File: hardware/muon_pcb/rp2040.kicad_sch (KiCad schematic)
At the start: 36 parts, among them J4 Micro_SD_Card_Det1, J5 Conn_01x02_Pin, SW4 SW_Push_Shielded, SW5 SW_Push_Shielded, U12 RP2040, U3 W25Q128JVS, Y3 ABM8-272-T3

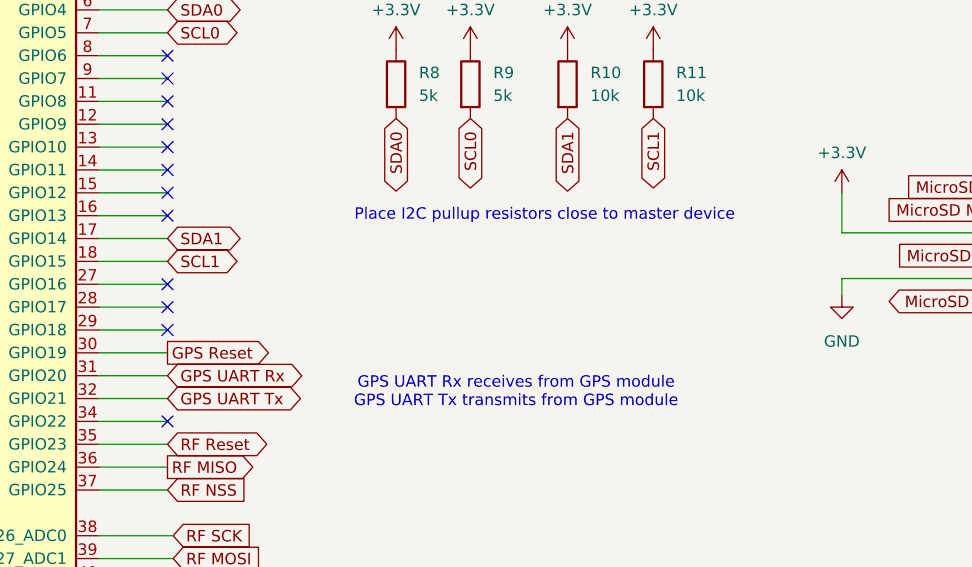
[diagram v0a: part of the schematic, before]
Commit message: uploaded preliminary pcb layout
need to research components to use (resistors & package size), buttons, test points, LEDs). also need to ask zach which ferrite bead he picked and about battery holder.
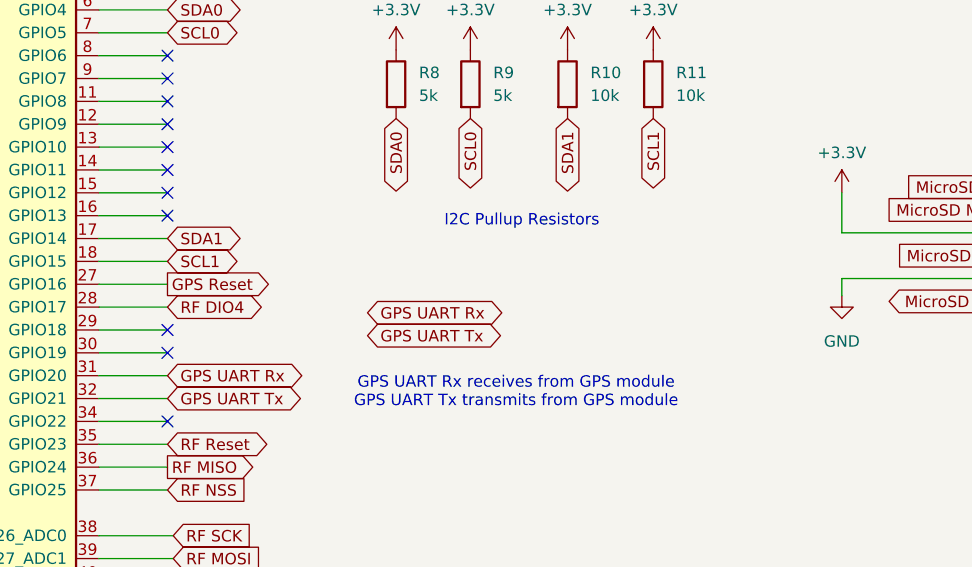
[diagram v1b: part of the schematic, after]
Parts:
- C1, C2: footprint Capacitor_SMD:C_0603_1608Metric -> Capacitor_SMD:C_0402_1005Metric
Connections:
- net GPS Reset: now also U12.27 (GPIO16); no longer U12.30 (GPIO19)
- net RF DIO4: now reaches U12.28 (GPIO17)
- no-connect marks 16 -> 15
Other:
- note added: "I2C Pullup Resistors"
- note removed: "Place I2C pullup resistors close to master device"
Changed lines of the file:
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@@
 	(generator_version "9.0")
 	(paper "A4")
-	(text "Place I2C pullup resistors close to master device"
-		(exclude_from_sim no)
-		(at 167.005 128.905 0)
-		(effects
-			(font
-				(size 1.27 1.27)
-			)
-		)
-	)
 	(text "Make sure C10 is close to pin 44 of RP2040"
 		(exclude_from_sim no)
@@
 		)
 	)
+	(text "I2C Pullup Resistors"
+		(exclude_from_sim no)
+		(at 164.465 129.54 0)
+		(effects
+			(font
+				(size 1.27 1.27)
+			)
+		)
+	)
 	(text "make sure diode used is\nexactly same one as used in proves kit"
 		(exclude_from_sim no)
@@
 	)
 	(no_connect
-		(at 125.095 136.525)
-	)
-	(no_connect
-		(at 125.095 139.065)
-	)
-	(no_connect
 		(at 125.095 123.825)
 	)
@@
 	)
 	(no_connect
+		(at 125.095 144.145)
+	)
+	(no_connect
 		(at 227.33 123.19)
 	)
@@
 		)
 	)
+	(global_label "RF DIO4"
+		(shape bidirectional)
+		(at 125.095 139.065 0)
+		(fields_autoplaced yes)
+		(effects
+			(font
+				(size 1.27 1.27)
+			)
+			(justify left)
+		)
+		(property "Intersheetrefs" "${INTERSHEET_REFS}"
+			(at 136.9325 139.065 0)
+			(effects
+				(font
+					(size 1.27 1.27)
+				)
+				(justify left)
+				(hide yes)
+			)
+		)
+	)
 	(global_label "RF SCK"
 		(shape input)
@@
 		)
 	)
-	(global_label "USB_DM"
-		(shape bidirectional)
-		(at 136.525 88.265 0)
+	(global_label "GPS Reset"
+		(shape output)
+		(at 125.095 136.525 0)
 		(fields_autoplaced yes)
 		(effects
 			(font
 				(size 1.27 1.27)
-				(thickness 0.1588)
 			)
 			(justify left)
 		)
 		(property "Intersheetrefs" "${INTERSHEET_REFS}"
-			(at 148.1205 88.265 0)
+			(at 137.9983 136.525 0)
 			(effects
 				(font
@@
 		)
 	)
-	(global_label "GPS Reset"
-		(shape output)
-		(at 125.095 144.145 0)
+	(global_label "USB_DM"
+		(shape bidirectional)
+		(at 136.525 88.265 0)
 		(fields_autoplaced yes)
 		(effects
 			(font
 				(size 1.27 1.27)
+				(thickness 0.1588)
 			)
 			(justify left)
 		)
 		(property "Intersheetrefs" "${INTERSHEET_REFS}"
-			(at 137.9983 144.145 0)
+			(at 148.1205 88.265 0)
 			(effects
 				(font
@@
 		)
 	)
+	(global_label "GPS UART Tx"
+		(shape bidirectional)
+		(at 147.32 142.24 0)
+		(fields_autoplaced yes)
+		(effects
+			(font
+				(size 1.27 1.27)
+			)
+			(justify left)
+		)
+		(property "Intersheetrefs" "${INTERSHEET_REFS}"
+			(at 163.7536 142.24 0)
+			(effects
+				(font
+					(size 1.27 1.27)
+				)
+				(justify left)
+				(hide yes)
+			)
+		)
+	)
 	(global_label "MicroSD CS"
 		(shape output)
@@
 		)
 	)
+	(global_label "GPS UART Rx"
+		(shape bidirectional)
+		(at 147.32 139.7 0)
+		(fields_autoplaced yes)
+		(effects
+			(font
+				(size 1.27 1.27)
+			)
+			(justify left)
+		)
+		(property "Intersheetrefs" "${INTERSHEET_REFS}"
+			(at 164.056 139.7 0)
+			(effects
+				(font
+					(size 1.27 1.27)
+				)
+				(justify left)
+				(hide yes)
+			)
+		)
+	)
 	(global_label "MicroSD CLK"
 		(shape input)
@@
 			)
 		)
-		(property "Footprint" "Capacitor_SMD:C_0603_1608Metric"
+		(property "Footprint" "Capacitor_SMD:C_0402_1005Metric"
 			(at 53.6702 74.295 0)
 			(effects
@@
 			)
 		)
-		(property "Footprint" "Capacitor_SMD:C_0603_1608Metric"
+		(property "Footprint" "Capacitor_SMD:C_0402_1005Metric"
 			(at 117.8052 73.025 0)
 			(effects

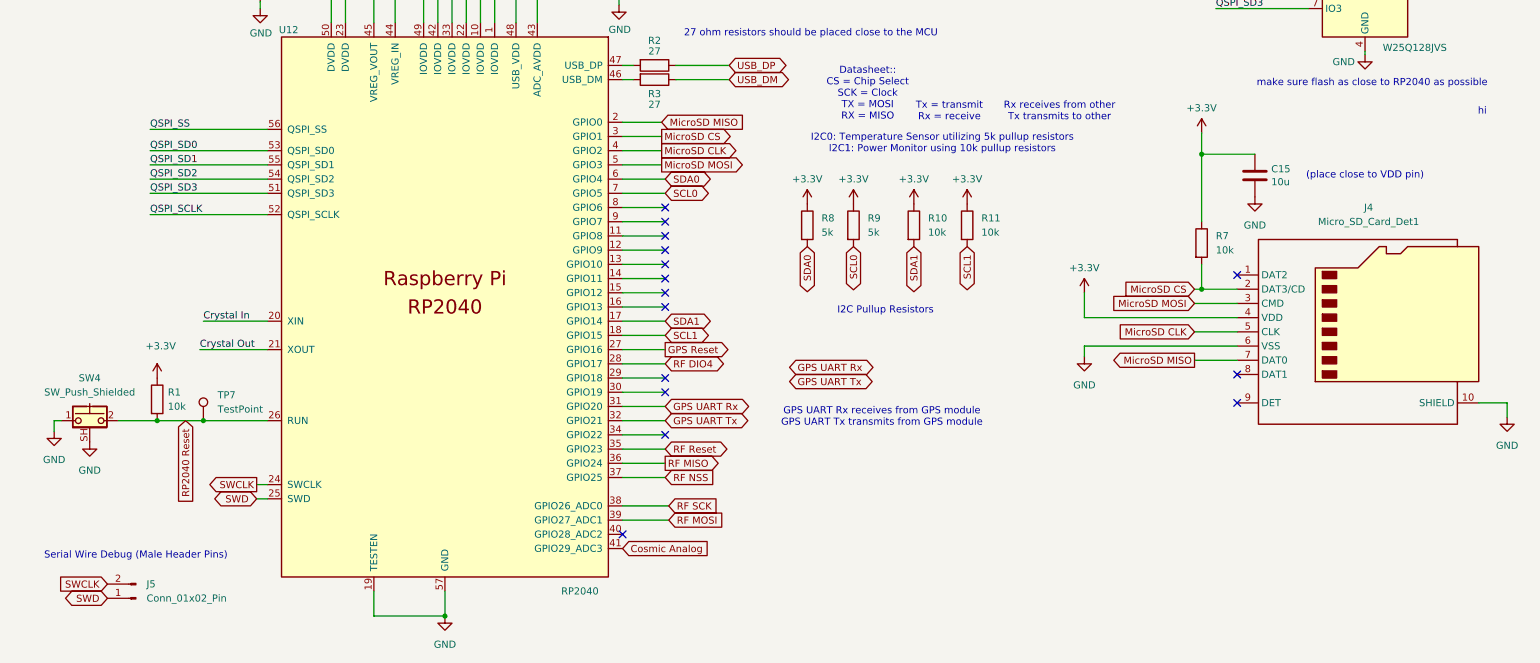
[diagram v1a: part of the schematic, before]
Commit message: uploaded pcb layout using proves edge cuts
-proves edge cuts with mounting holes
-added credits
-used correct sizes for resistors (based on components picked for resistors)
-to do: pick button, put in df11 connector to supply 5V, determine led being used and resistor values, make sure led wont explode
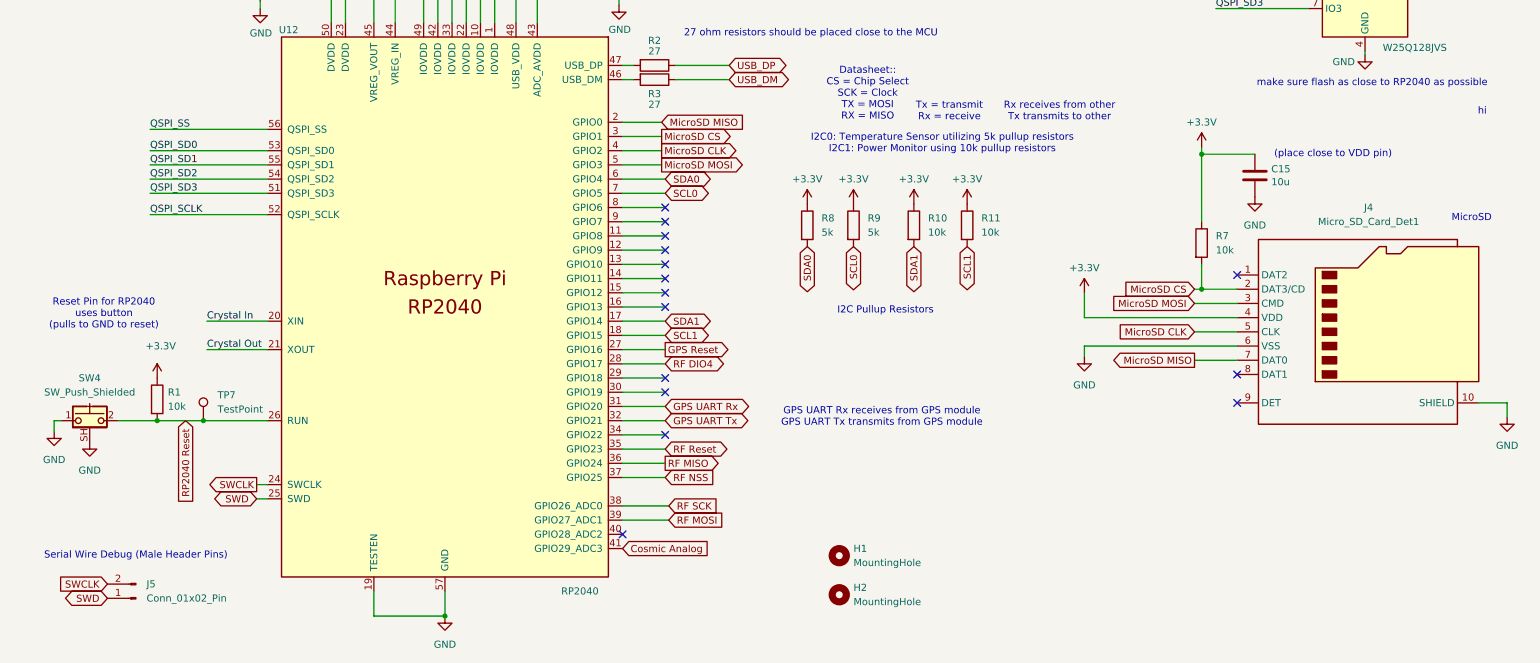
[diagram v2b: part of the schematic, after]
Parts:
- added H1, H2: MountingHole, symbol Mechanical:MountingHole
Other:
- note added: "MicroSD"
- note added: "Reset Pin for RP2040 uses button (pulls to GND to reset)"
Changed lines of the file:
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@@
 		)
 	)
+	(text "MicroSD"
+		(exclude_from_sim no)
+		(at 269.24 113.03 0)
+		(effects
+			(font
+				(size 1.27 1.27)
+			)
+		)
+	)
+	(text "Reset Pin for RP2040 \nuses button\n(pulls to GND to reset)"
+		(exclude_from_sim no)
+		(at 24.765 130.175 0)
+		(effects
+			(font
+				(size 1.27 1.27)
+			)
+		)
+	)
 	(text "make sure flash as close to RP2040 as possible"
 		(exclude_from_sim no)
@@
 	(text "(place close to VDD pin)"
 		(exclude_from_sim no)
-		(at 250.19 105.41 0)
+		(at 244.475 101.6 0)
 		(effects
 			(font
@@
 	(wire
 		(pts
-			(xy 220.98 97.79) (xy 220.98 101.6)
+			(xy 220.98 100.33) (xy 220.98 101.6)
 		)
 		(stroke
@@
 	(wire
 		(pts
-			(xy 42.545 131.445) (xy 53.975 131.445)
+			(xy 43.18 131.445) (xy 53.975 131.445)
 		)
 		(stroke
@@
 	(wire
 		(pts
-			(xy 41.91 136.525) (xy 53.975 136.525)
+			(xy 43.18 136.525) (xy 53.975 136.525)
 		)
 		(stroke
@@
 	)
 	(label "Crystal Out"
-		(at 41.91 136.525 0)
+		(at 43.18 136.525 0)
 		(effects
 			(font
@@
 	)
 	(label "Crystal In"
-		(at 42.545 131.445 0)
+		(at 43.18 131.445 0)
 		(effects
 			(font
@@
 		)
 	)
-	(global_label "GPS UART Tx"
-		(shape bidirectional)
-		(at 147.32 142.24 0)
-		(fields_autoplaced yes)
-		(effects
-			(font
-				(size 1.27 1.27)
-			)
-			(justify left)
-		)
-		(property "Intersheetrefs" "${INTERSHEET_REFS}"
-			(at 163.7536 142.24 0)
-			(effects
-				(font
-					(size 1.27 1.27)
-				)
-				(justify left)
-				(hide yes)
-			)
-		)
-	)
 	(global_label "MicroSD CS"
 		(shape output)
@@
 		)
 	)
-	(global_label "GPS UART Rx"
-		(shape bidirectional)
-		(at 147.32 139.7 0)
-		(fields_autoplaced yes)
-		(effects
-			(font
-				(size 1.27 1.27)
-			)
-			(justify left)
-		)
-		(property "Intersheetrefs" "${INTERSHEET_REFS}"
-			(at 164.056 139.7 0)
-			(effects
-				(font
-					(size 1.27 1.27)
-				)
-				(justify left)
-				(hide yes)
-			)
-		)
-	)
 	(global_label "MicroSD CLK"
 		(shape input)
@@
 	)
 	(symbol
+		(lib_id "Mechanical:MountingHole")
+		(at 156.21 180.34 0)
+		(unit 1)
+		(exclude_from_sim yes)
+		(in_bom no)
+		(on_board yes)
+		(dnp no)
+		(fields_autoplaced yes)
+		(property "Reference" "H2"
+			(at 158.75 179.0699 0)
+			(effects
+				(font
+					(size 1.27 1.27)
+				)
+				(justify left)
+			)
+		)
+		(property "Value" "MountingHole"
+			(at 158.75 181.6099 0)
+			(effects
+				(font
+					(size 1.27 1.27)
+				)
+				(justify left)
+			)
+		)
+		(property "Footprint" ""
+			(at 156.21 180.34 0)
+			(effects
+				(font
+					(size 1.27 1.27)
+				)
+				(hide yes)
+			)
+		)
+		(property "Datasheet" "~"
+			(at 156.21 180.34 0)
+			(effects
+				(font
+					(size 1.27 1.27)
+				)
+				(hide yes)
+			)
+		)
+		(property "Description" "Mounting Hole without connection"
+			(at 156.21 180.34 0)
+			(effects
+				(font
+					(size 1.27 1.27)
+				)
+				(hide yes)
+			)
+		)
+		(instances
+			(project "og_pcb"
+				(path "/e4ef350a-b140-44e0-8bc3-973fc24bf90a/06e07132-39d3-4769-b65c-2c1064b388d8"
+					(reference "H2")
+					(unit 1)
+				)
+			)
+		)
+	)
+	(symbol
 		(lib_id "Device:R")
 		(at 123.19 85.725 270)
@@
 	(symbol
 		(lib_id "power:+3.3V")
-		(at 220.98 97.79 0)
+		(at 220.98 100.33 0)
 		(unit 1)
 		(exclude_from_sim no)
@@
 		(fields_autoplaced yes)
 		(property "Reference" "#PWR0134"
-			(at 220.98 101.6 0)
+			(at 220.98 104.14 0)
 			(effects
 				(font
@@
 		)
 		(property "Value" "+3.3V"
-			(at 220.98 93.345 0)
+			(at 220.98 95.885 0)
 			(effects
 				(font
@@
 		)
 		(property "Footprint" ""
-			(at 220.98 97.79 0)
+			(at 220.98 100.33 0)
 			(effects
 				(font
@@
 		)
 		(property "Datasheet" ""
-			(at 220.98 97.79 0)
+			(at 220.98 100.33 0)
 			(effects
 				(font
@@
 		)
 		(property "Description" "Power symbol creates a global label with name \"+3.3V\""
-			(at 220.98 97.79 0)
+			(at 220.98 100.33 0)
 			(effects
 				(font
@@
 					(unit 1)
 				)
+			)
+		)
+	)
+	(symbol
+		(lib_id "Mechanical:MountingHole")
+		(at 156.21 173.355 0)
+		(unit 1)
+		(exclude_from_sim yes)
+		(in_bom no)
+		(on_board yes)
+		(dnp no)
+		(fields_autoplaced yes)
+		(property "Reference" "H1"
+			(at 158.75 172.0849 0)
+			(effects
+				(font
+					(size 1.27 1.27)
+				)
+				(justify left)
+			)
+		)
+		(property "Value" "MountingHole"
+			(at 158.75 174.6249 0)
+			(effects
+				(font
+					(size 1.27 1.27)
+				)
+				(justify left)
+			)
+		)
+		(property "Footprint" ""
+			(at 156.21 173.355 0)
+			(effects
+				(font
+					(size 1.27 1.27)
+				)
+				(hide yes)
+			)
+		)
+		(property "Datasheet" "~"
+			(at 156.21 173.355 0)
+			(effects
+				(font
+					(size 1.27 1.27)
+				)
+				(hide yes)
+			)
+		)
+		(property "Description" "Mounting Hole without connection"
+			(at 156.21 173.355 0)
+			(effects
+				(font
+					(size 1.27 1.27)
+				)
+				(hide yes)
+			)
+		)
+		(instances
+			(project ""
+				(path "/e4ef350a-b140-44e0-8bc3-973fc24bf90a/06e07132-39d3-4769-b65c-2c1064b388d8"
+					(reference "H1")
+					(unit 1)
+				)

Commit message: updated pcb layout
fixed SMA connector footprint, assigned bom to all components except resistors and test points. resistors alr decided on, only need to assign
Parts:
- SW4, SW5: footprint Button_Switch_SMD:SW_Push_1P1T-SH_NO_CK_KMR2xxG -> Button_Switch_SMD:SW_Push_1P1T_NO_CK_KMR2
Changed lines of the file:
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@@
 			)
 		)
-		(property "Footprint" "Button_Switch_SMD:SW_Push_1P1T-SH_NO_CK_KMR2xxG"
+		(property "Footprint" "Button_Switch_SMD:SW_Push_1P1T_NO_CK_KMR2"
 			(at 173.99 50.8 0)
 			(effects
@@
 			)
 		)
-		(property "Footprint" "Button_Switch_SMD:SW_Push_1P1T-SH_NO_CK_KMR2xxG"
+		(property "Footprint" "Button_Switch_SMD:SW_Push_1P1T_NO_CK_KMR2"
 			(at 22.225 144.145 0)
 			(effects
@@
 			)
 		)
-		(property "Datasheet" "https://datasheet.lcsc.com/lcsc/2110151630_XKB-Connectivity-XKTF-015-N_C381082.pdf"
+		(property "Datasheet" "https://www.molex.com/en-us/products/part-detail/5033981892?display=pdf"
 			(at 250.19 130.81 0)
 			(effects
